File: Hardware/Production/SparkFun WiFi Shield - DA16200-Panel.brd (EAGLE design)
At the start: 200.2 x 127.3 mm, 960 parts, among them J1 CORTEX_JTAG_DEBUG, J11 CORTEX_JTAG_DEBUG, J13 QWIIC_RA, J16 CORTEX_JTAG_DEBUG, J18 QWIIC_RA, J21 CORTEX_JTAG_DEBUG, J23 QWIIC_RA, J26 CORTEX_JTAG_DEBUG, J28 QWIIC_RA, J3 QWIIC_RA, J6 CORTEX_JTAG_DEBUG, J8 QWIIC_RA, U1 DA16200MOD, U2 DA16200MOD, U3 DA16200MOD, U4 DA16200MOD, U5 DA16200MOD, U6 DA16200MOD

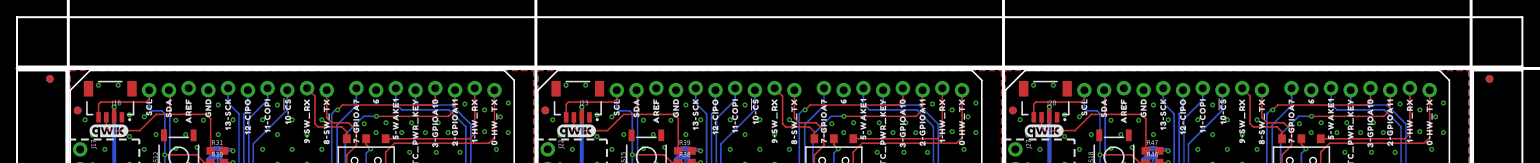
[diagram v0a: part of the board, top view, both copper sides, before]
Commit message: Panel update
Moved fiducials away from v-score
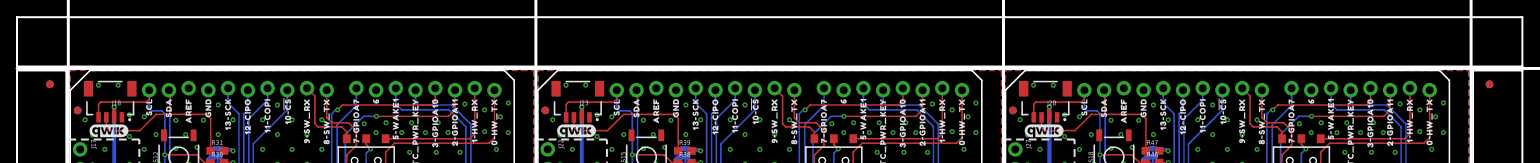
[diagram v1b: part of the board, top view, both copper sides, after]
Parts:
- moved E$1 0.70 mm to (-2.62, 105.4)
- moved E$2 0.70 mm to (-2.62, 105.4)
- moved E$3 0.70 mm to (182.7, 105.4)
- moved E$4 0.70 mm to (182.7, 105.4)
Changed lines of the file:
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@@
 <layer number="19" name="Unrouted" color="6" fill="1" visible="yes" active="yes"/>
 <layer number="20" name="Dimension" color="24" fill="1" visible="yes" active="yes"/>
-<layer number="21" name="tPlace" color="7" fill="1" visible="yes" active="yes"/>
-<layer number="22" name="bPlace" color="7" fill="1" visible="yes" active="yes"/>
+<layer number="21" name="tPlace" color="16" fill="1" visible="yes" active="yes"/>
+<layer number="22" name="bPlace" color="14" fill="1" visible="yes" active="yes"/>
 <layer number="23" name="tOrigins" color="15" fill="1" visible="yes" active="yes"/>
 <layer number="24" name="bOrigins" color="15" fill="1" visible="yes" active="yes"/>
-<layer number="25" name="tNames" color="7" fill="1" visible="yes" active="yes"/>
-<layer number="26" name="bNames" color="7" fill="1" visible="yes" active="yes"/>
-<layer number="27" name="tValues" color="7" fill="1" visible="yes" active="yes"/>
-<layer number="28" name="bValues" color="7" fill="1" visible="yes" active="yes"/>
+<layer number="25" name="tNames" color="7" fill="1" visible="no" active="yes"/>
+<layer number="26" name="bNames" color="7" fill="1" visible="no" active="yes"/>
+<layer number="27" name="tValues" color="7" fill="1" visible="no" active="yes"/>
+<layer number="28" name="bValues" color="7" fill="1" visible="no" active="yes"/>
 <layer number="29" name="tStop" color="7" fill="3" visible="yes" active="yes"/>
-<layer number="30" name="bStop" color="7" fill="6" visible="yes" active="yes"/>
-<layer number="31" name="tCream" color="7" fill="4" visible="yes" active="yes"/>
-<layer number="32" name="bCream" color="7" fill="5" visible="yes" active="yes"/>
-<layer number="33" name="tFinish" color="6" fill="3" visible="yes" active="yes"/>
-<layer number="34" name="bFinish" color="6" fill="6" visible="yes" active="yes"/>
-<layer number="35" name="tGlue" color="7" fill="4" visible="yes" active="yes"/>
-<layer number="36" name="bGlue" color="7" fill="5" visible="yes" active="yes"/>
-<layer number="37" name="tTest" color="7" fill="1" visible="yes" active="yes"/>
-<layer number="38" name="bTest" color="7" fill="1" visible="yes" active="yes"/>
-<layer number="39" name="tKeepout" color="4" fill="11" visible="yes" active="yes"/>
-<layer number="40" name="bKeepout" color="1" fill="11" visible="yes" active="yes"/>
-<layer number="41" name="tRestrict" color="4" fill="10" visible="yes" active="yes"/>
-<layer number="42" name="bRestrict" color="1" fill="10" visible="yes" active="yes"/>
-<layer number="43" name="vRestrict" color="2" fill="10" visible="yes" active="yes"/>
-<layer number="44" name="Drills" color="7" fill="1" visible="yes" active="yes"/>
+<layer number="30" name="bStop" color="7" fill="6" visible="no" active="yes"/>
+<layer number="31" name="tCream" color="7" fill="4" visible="no" active="yes"/>
+<layer number="32" name="bCream" color="7" fill="5" visible="no" active="yes"/>
+<layer number="33" name="tFinish" color="6" fill="3" visible="no" active="yes"/>
+<layer number="34" name="bFinish" color="6" fill="6" visible="no" active="yes"/>
+<layer number="35" name="tGlue" color="7" fill="4" visible="no" active="yes"/>
+<layer number="36" name="bGlue" color="7" fill="5" visible="no" active="yes"/>
+<layer number="37" name="tTest" color="7" fill="1" visible="no" active="yes"/>
+<layer number="38" name="bTest" color="7" fill="1" visible="no" active="yes"/>
+<layer number="39" name="tKeepout" color="4" fill="11" visible="no" active="yes"/>
+<layer number="40" name="bKeepout" color="1" fill="11" visible="no" active="yes"/>
+<layer number="41" name="tRestrict" color="4" fill="10" visible="no" active="yes"/>
+<layer number="42" name="bRestrict" color="1" fill="10" visible="no" active="yes"/>
+<layer number="43" name="vRestrict" color="2" fill="10" visible="no" active="yes"/>
+<layer number="44" name="Drills" color="7" fill="1" visible="no" active="yes"/>
 <layer number="45" name="Holes" color="7" fill="1" visible="yes" active="yes"/>
 <layer number="46" name="Milling" color="3" fill="1" visible="yes" active="yes"/>
-<layer number="47" name="Measures" color="7" fill="1" visible="yes" active="yes"/>
-<layer number="48" name="Document" color="7" fill="1" visible="yes" active="yes"/>
-<layer number="49" name="Reference" color="7" fill="1" visible="yes" active="yes"/>
+<layer number="47" name="Measures" color="7" fill="1" visible="no" active="yes"/>
+<layer number="48" name="Document" color="7" fill="1" visible="no" active="yes"/>
+<layer number="49" name="Reference" color="7" fill="1" visible="no" active="yes"/>
 <layer number="50" name="dxf" color="7" fill="1" visible="no" active="no"/>
-<layer number="51" name="tDocu" color="7" fill="1" visible="yes" active="yes"/>
-<layer number="52" name="bDocu" color="7" fill="1" visible="yes" active="yes"/>
+<layer number="51" name="tDocu" color="6" fill="1" visible="yes" active="yes"/>
+<layer number="52" name="bDocu" color="7" fill="1" visible="no" active="yes"/>
 <layer number="53" name="tGND_GNDA" color="7" fill="9" visible="no" active="no"/>
 <layer number="54" name="bGND_GNDA" color="1" fill="9" visible="no" active="no"/>
@@
 <element name="U$713" library="output" package="2#GPIOA110" value="" x="169.926" y="104.14" smashed="yes" rot="MR90"/>
 <element name="U$714" library="output" package="2#GPIOA110" value="" x="169.926" y="104.14" smashed="yes" rot="R90"/>
-<element name="E$1" library="SparkFun-Aesthetics" package="FIDUCIAL-1X2" value="" x="-2.62381875" y="106.1085" smashed="yes"/>
-<element name="E$2" library="SparkFun-Aesthetics" package="FIDUCIAL-1X2" value="" x="-2.62381875" y="106.1085" smashed="yes" rot="MR0"/>
-<element name="E$3" library="SparkFun-Aesthetics" package="FIDUCIAL-1X2" value="" x="182.70981875" y="106.1085" smashed="yes"/>
-<element name="E$4" library="SparkFun-Aesthetics" package="FIDUCIAL-1X2" value="" x="182.70981875" y="106.1085" smashed="yes" rot="MR0"/>
+<element name="E$1" library="SparkFun-Aesthetics" package="FIDUCIAL-1X2" value="" x="-2.62381875" y="105.41" smashed="yes"/>
+<element name="E$2" library="SparkFun-Aesthetics" package="FIDUCIAL-1X2" value="" x="-2.62381875" y="105.41" smashed="yes" rot="MR0"/>
+<element name="E$3" library="SparkFun-Aesthetics" package="FIDUCIAL-1X2" value="" x="182.70981875" y="105.41" smashed="yes"/>
+<element name="E$4" library="SparkFun-Aesthetics" package="FIDUCIAL-1X2" value="" x="182.70981875" y="105.41" smashed="yes" rot="MR0"/>
 <element name="E$5" library="SparkFun-Retired" package="FIDUCIAL-1.5X3" value="" x="-2.62381875" y="6.858" smashed="yes"/>
 <element name="E$6" library="SparkFun-Retired" package="FIDUCIAL-1.5X3" value="" x="-2.62381875" y="6.858" smashed="yes" rot="MR0"/>
